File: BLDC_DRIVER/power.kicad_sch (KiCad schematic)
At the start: 17 parts, among them J1 Screw_Terminal_01x02, U1 LM3404HVMA, U102 LMR51430, U3 LDI1117-3.3H

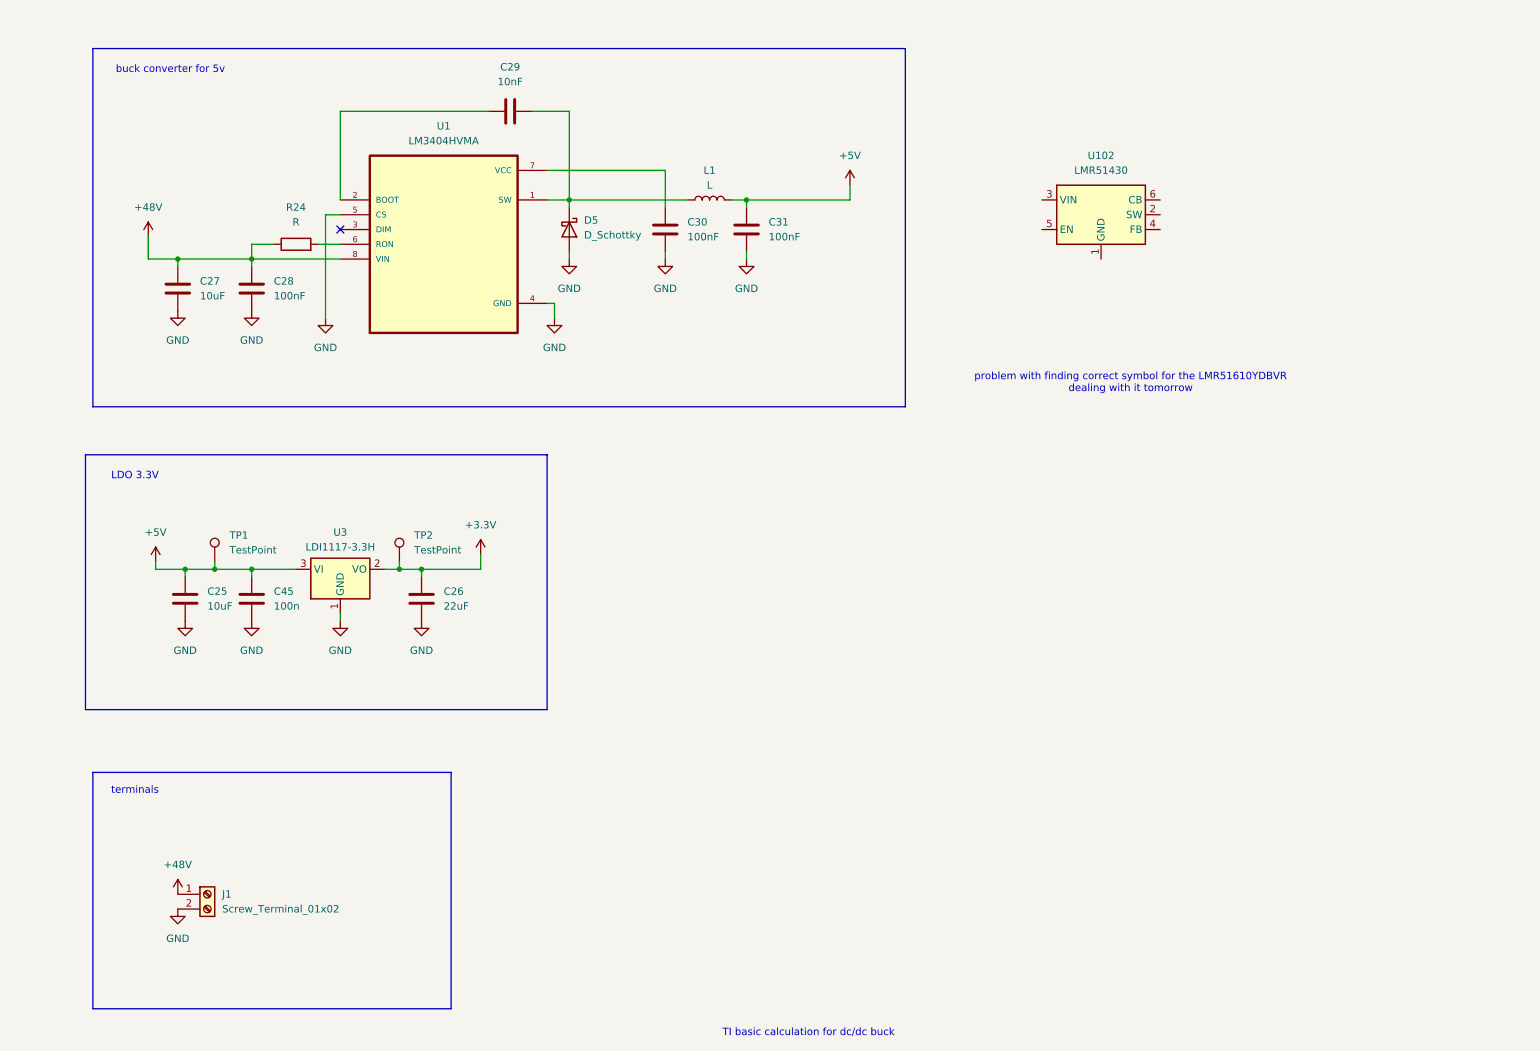
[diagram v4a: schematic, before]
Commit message: buck changed and calculated
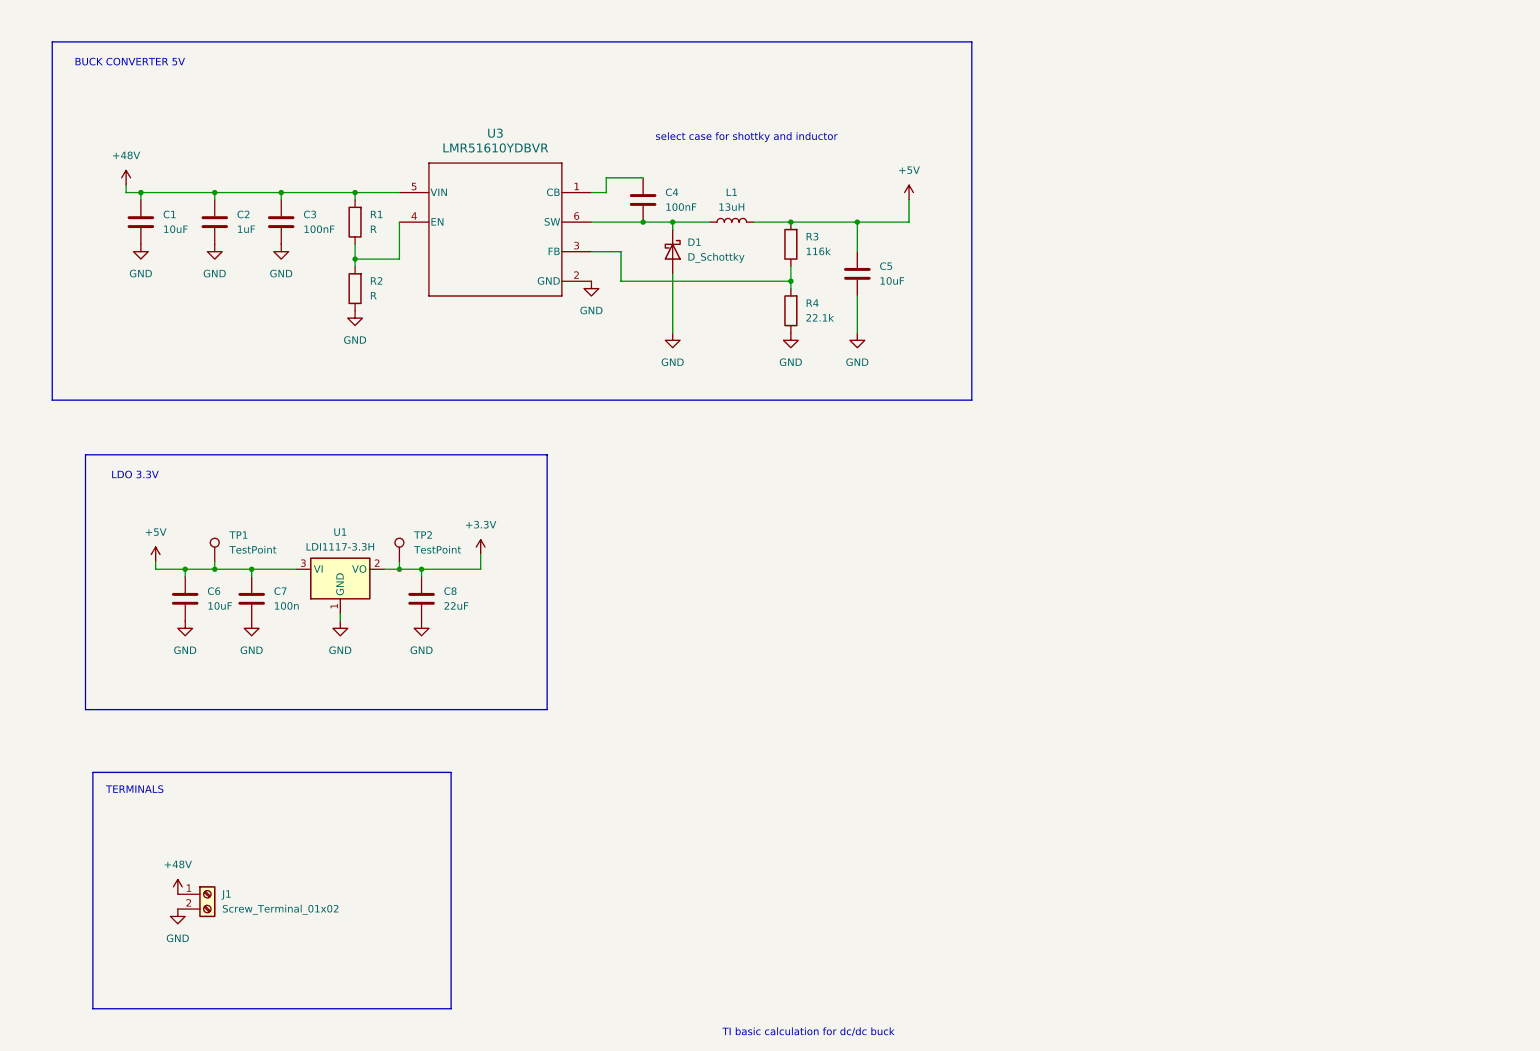
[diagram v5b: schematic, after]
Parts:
- removed C29: 10nF, symbol Device:C
- removed C30, C31: 100nF, symbol Device:C
- removed U1: LM3404HVMA, LM3404:SOIC127P599X175-8N, symbol LM3404:LM3404HVMA
- removed U102: LMR51430, Package_TO_SOT_SMD:SOT-23-6, symbol Regulator_Switching:LMR51430
- added C2: 1uF, Capacitor_SMD:C_0805_2012Metric_Pad1.18x1.45mm_HandSolder, symbol Device:C
- added C4: 100nF, Capacitor_SMD:C_0603_1608Metric_Pad1.08x0.95mm_HandSolder, symbol Device:C
- added C5: 10uF, Capacitor_SMD:C_0805_2012Metric_Pad1.18x1.45mm_HandSolder, symbol Device:C
- added R2: R, Resistor_SMD:R_0603_1608Metric_Pad0.98x0.95mm_HandSolder, symbol Device:R
- added R3: 116k, Resistor_SMD:R_0603_1608Metric_Pad0.98x0.95mm_HandSolder, symbol Device:R
- added R4: 22.1k, Resistor_SMD:R_0603_1608Metric_Pad0.98x0.95mm_HandSolder, symbol Device:R
- added U3: LMR51610YDBVR, Package_TO_SOT_SMD:SOT-23-6, symbol LMR51610YDBVR:LMR51610YDBVR
- C1: renamed from C27; footprint (none) -> Capacitor_SMD:C_0805_2012Metric_Pad1.18x1.45mm_HandSolder
- C3: renamed from C28; footprint (none) -> Capacitor_SMD:C_0805_2012Metric_Pad1.18x1.45mm_HandSolder
- C6: renamed from C25; footprint (none) -> Capacitor_SMD:C_0805_2012Metric_Pad1.18x1.45mm_HandSolder
- C7: renamed from C45; footprint (none) -> Capacitor_SMD:C_0603_1608Metric_Pad1.08x0.95mm_HandSolder
- C8: renamed from C26; footprint (none) -> Capacitor_SMD:C_0805_2012Metric_Pad1.18x1.45mm_HandSolder
- L1: value L -> 13uH
- R1: renamed from R24; footprint (none) -> Resistor_SMD:R_0603_1608Metric_Pad0.98x0.95mm_HandSolder
- renumbered D5 to D1, U3 to U1
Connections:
- net +48V: now also R1.2, C2.1, U3.5 (VIN); no longer R1.1
- net +5V: now also C5.2, R3.2
- net GND: now also C2.2, C5.1, R2.1, R4.1, U3.2 (GND)
- net at D1.1 (K), L1.1: now also C4.1, U3.6 (SW)
- new net: R1.1, R2.2, U3.4 (EN)
- new net: R3.1, R4.2, U3.3 (FB)
- new net: C4.2, U3.1 (CB)
- no-connect marks 1 -> 0
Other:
- note added: "BUCK CONVERTER 5V"
- note added: "TERMINALS"
- note added: "select case for shottky and inductor"
- note removed: "buck converter for 5v"
- note removed: "problem with finding correct symbol for the LMR51610YDBVR dealing with it tomorrow"
- note removed: "terminals"
- moved on the sheet: C1, C3, D1, L1, R1

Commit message: fuses and missing footprints added, labels cleaned
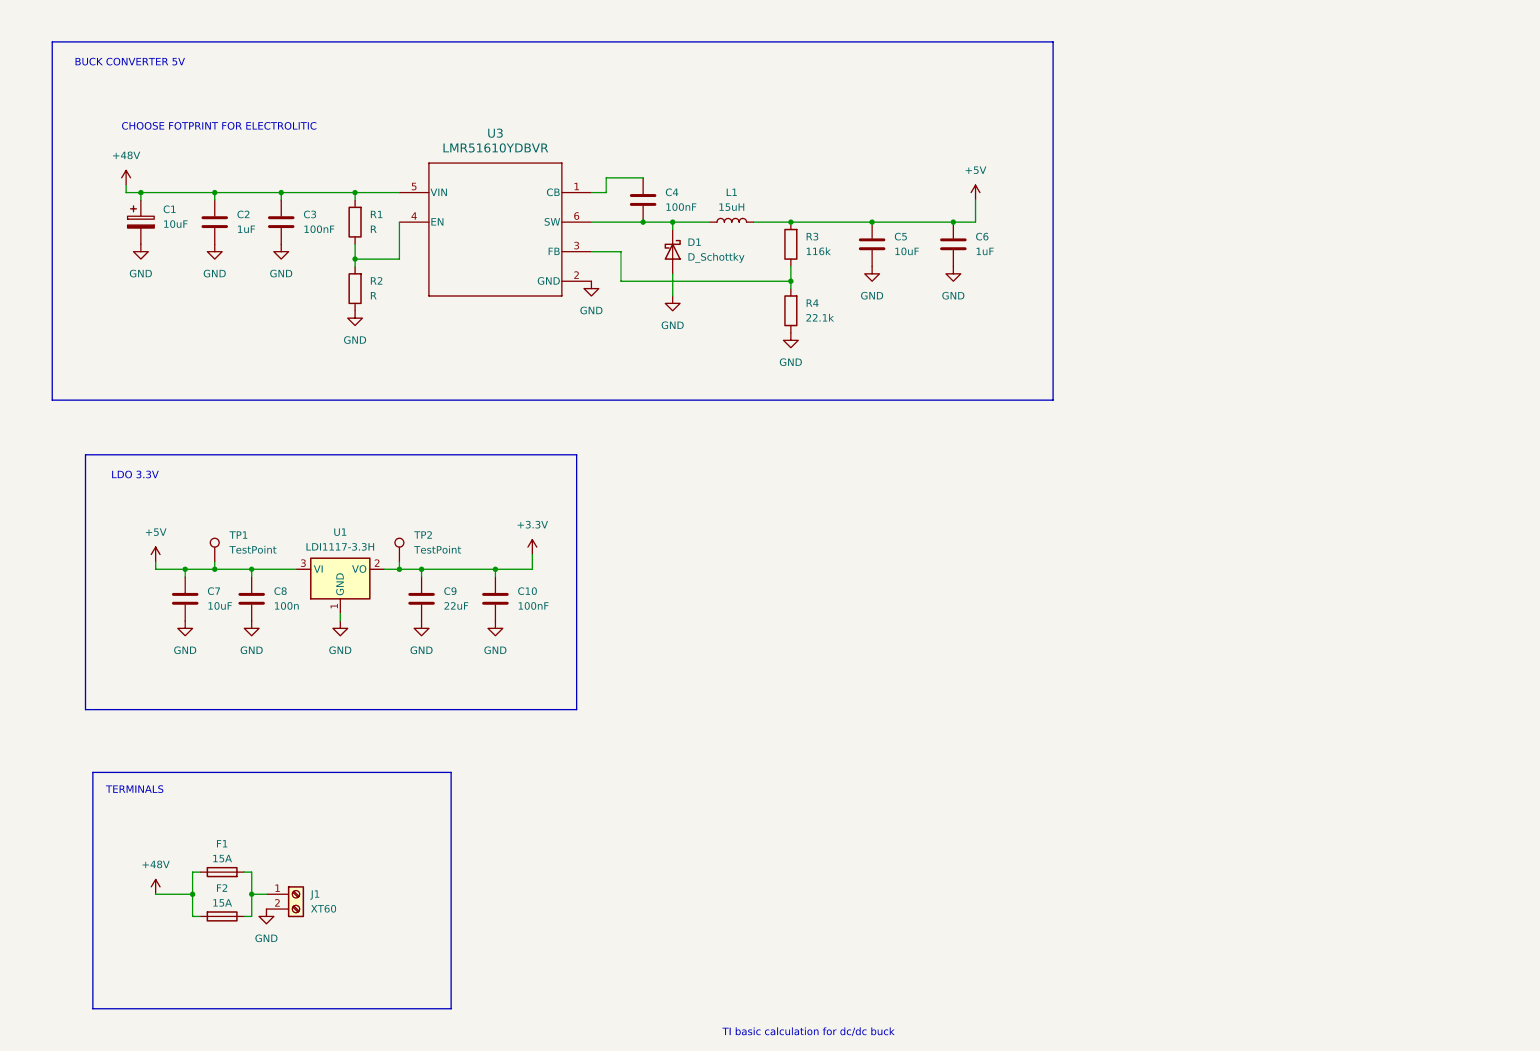
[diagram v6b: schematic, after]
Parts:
- removed C1: 10uF, Capacitor_SMD:C_0805_2012Metric_Pad1.18x1.45mm_HandSolder, symbol Device:C
- added C1: 10uF, symbol Device:C_Polarized
- added C10: 100nF, Capacitor_SMD:C_0805_2012Metric_Pad1.18x1.45mm_HandSolder, symbol Device:C
- added C6: 1uF, Capacitor_SMD:C_0805_2012Metric_Pad1.18x1.45mm_HandSolder, symbol Device:C
- added F1, F2: 15A, Fuse:Fuse_Blade_ATO_directSolder, symbol Device:Fuse
- D1: footprint (none) -> Diode_SMD:D_SMA
- J1: value Screw_Terminal_01x02 -> XT60; footprint Connector_AMASS:AMASS_XT60-F_1x02_P7.20mm_Vertical -> Connector_AMASS:AMASS_XT60-M_1x02_P7.20mm_Vertical
- L1: value 13uH -> 15uH; footprint (none) -> Inductor_SMD:L_APV_ANR6045
- renumbered C6 to C7, C7 to C8, C8 to C9
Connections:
- net +3.3V: now also C10.1
- net +48V: now also C1.1, F1.1, F2.2; no longer J1.1 (Pin_1)
- net +5V: now also C6.2
- net GND: now also C1.2, C10.2, C6.1
- new net: F1.2, F2.1, J1.1 (Pin_1)
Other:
- note added: "CHOOSE FOTPRINT FOR ELECTROLITIC"
- note removed: "select case for shottky and inductor"
- moved on the sheet: C5, J1

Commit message: finall motor driver
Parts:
- C1: footprint (none) -> EMVY101ARA101MKE0S:CAPAE1300X1400N
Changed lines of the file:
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@@
 			)
 		)
-		(property "Footprint" ""
+		(property "Footprint" "EMVY101ARA101MKE0S:CAPAE1300X1400N"
 			(at 40.3352 57.15 0)
 			(effects

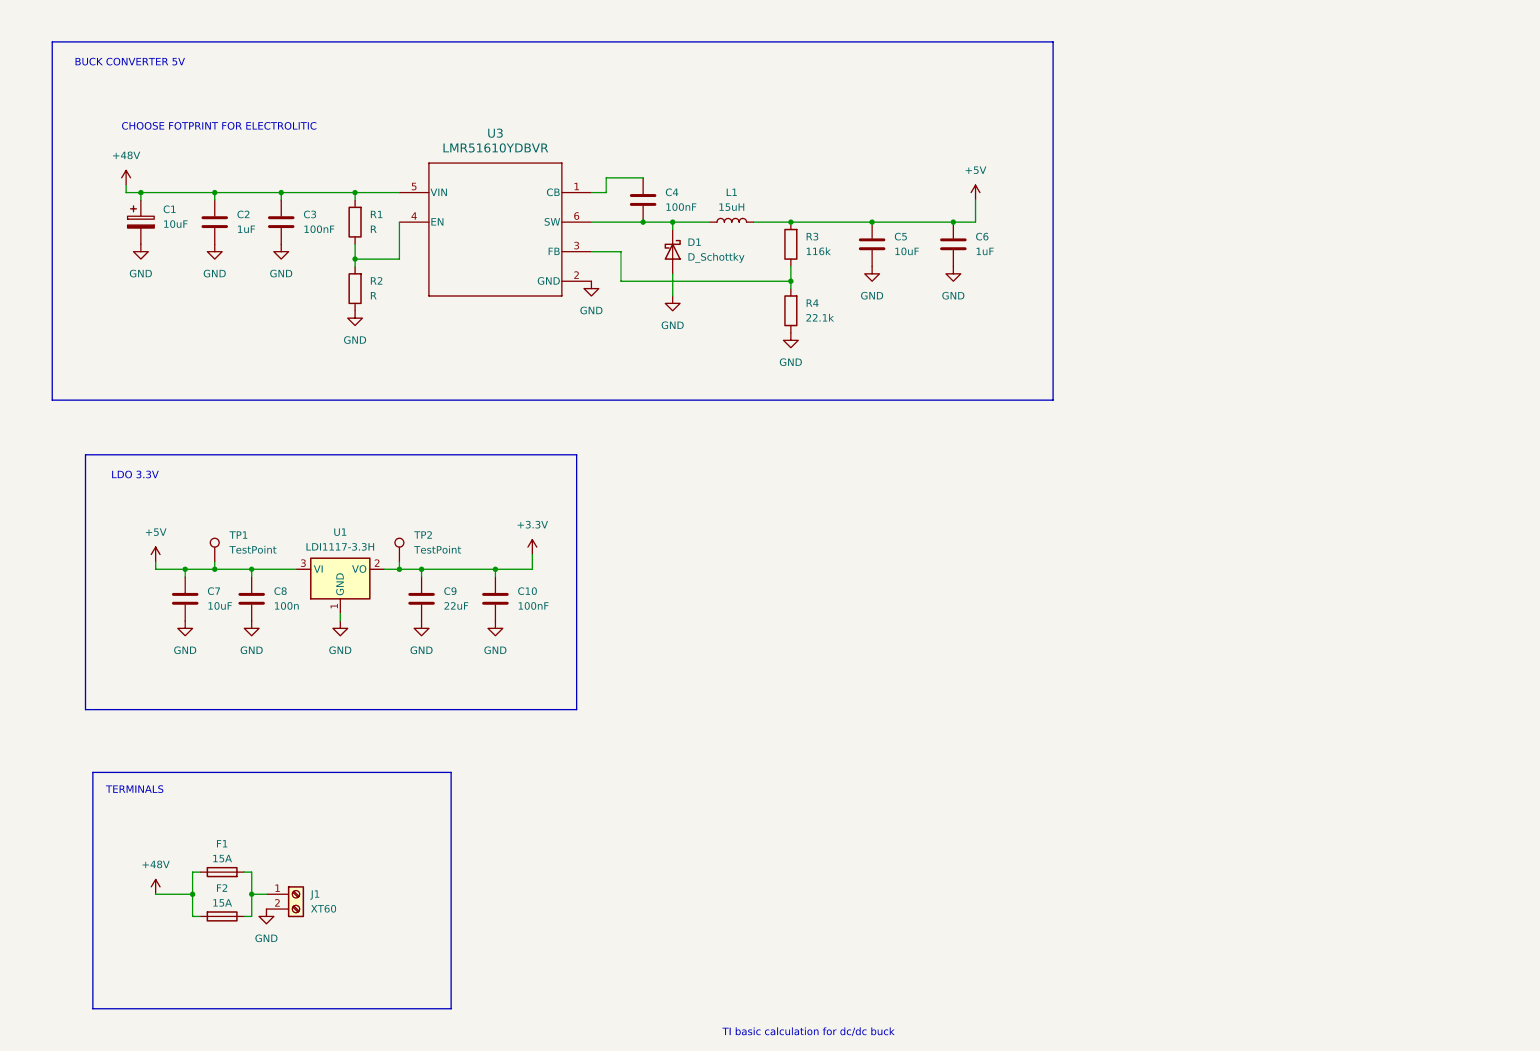
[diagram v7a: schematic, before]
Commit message: board constraints added
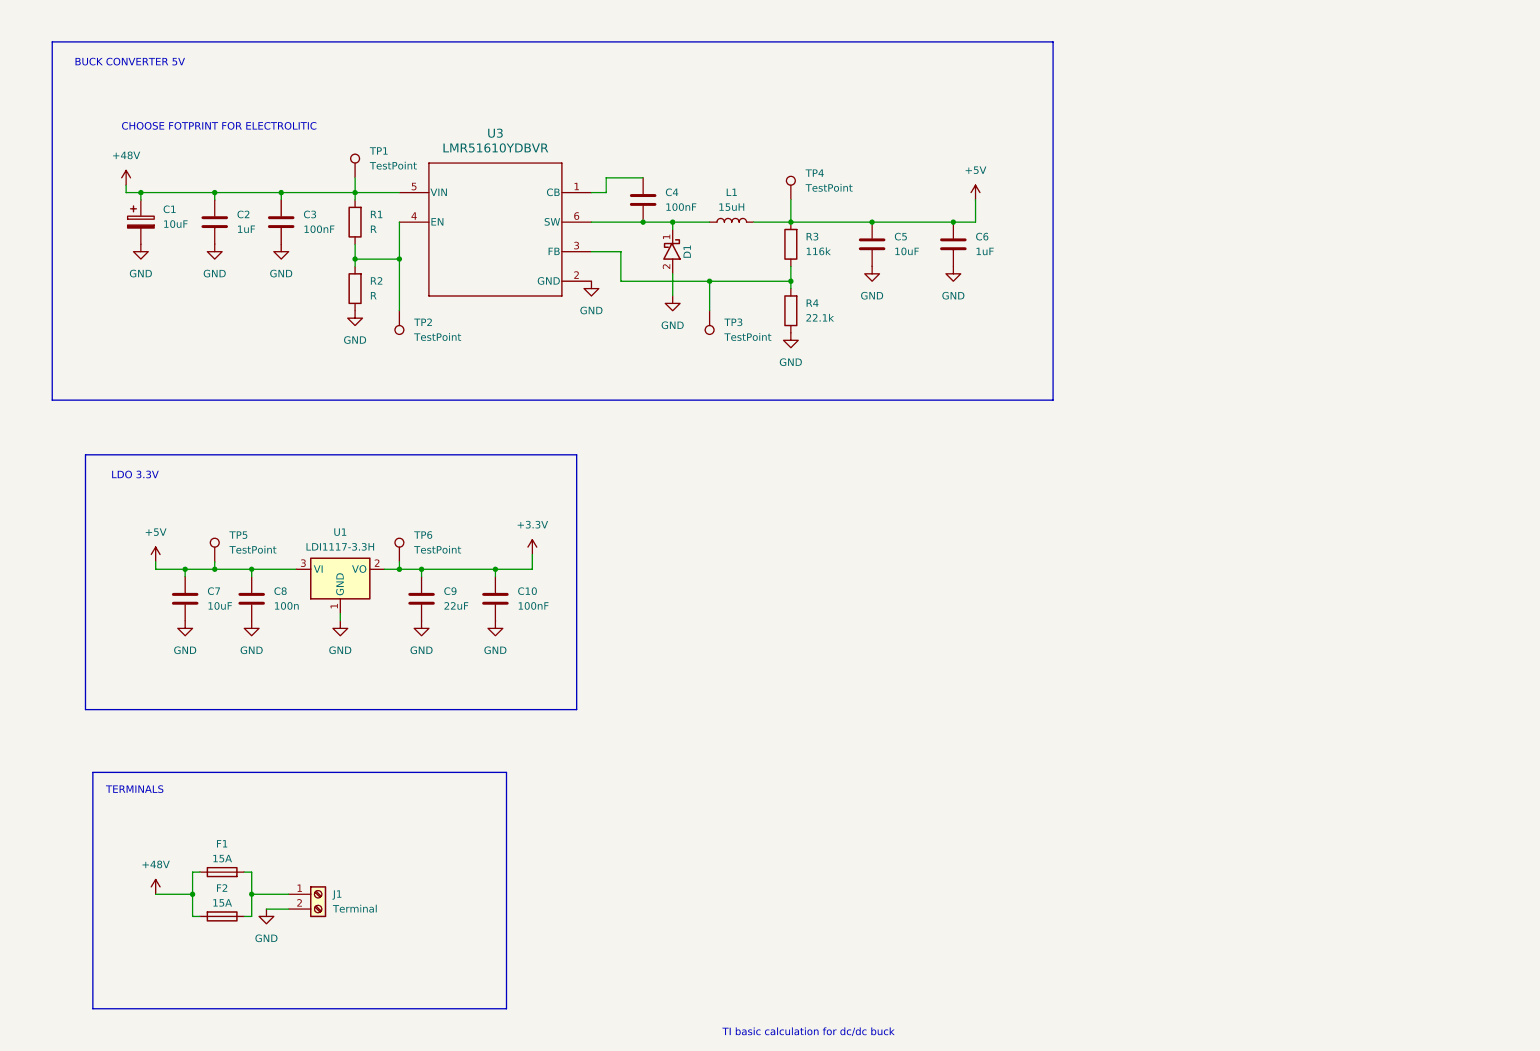
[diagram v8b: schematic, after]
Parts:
- removed D1: D_Schottky, Diode_SMD:D_SMA, symbol Device:D_Schottky
- added D1: SBR3U60P1-7, Diode_SMD:D_PowerDI-123, symbol SBR3U60P1-7:SBR3U60P1-7
- added TP1, TP2, TP3, TP4: TestPoint, TestPoint:TestPoint_Pad_D1.5mm, symbol Connector:TestPoint
- J1: value XT60 -> Terminal; footprint Connector_AMASS:AMASS_XT60-M_1x02_P7.20mm_Vertical -> TerminalBlock:TerminalBlock_Wuerth_691311400102_P7.62mm
- renumbered TP1 to TP5, TP2 to TP6
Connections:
- net +48V: now also TP1.1
- net +5V: now also TP4.1
- net GND: now also D1.2
- net at R1.1, R2.2, U3.4 (EN): now also TP2.1
- net at C4.1, L1.1, U3.6 (SW): now also D1.1
- net at R3.1, R4.2, U3.3 (FB): now also TP3.1
